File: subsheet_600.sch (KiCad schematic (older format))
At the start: 9 parts, among them U600 SIMM_30_PHY, U601 SIMM_30_PHY, U602 SIMM_30_PHY, U603 SIMM_30_PHY

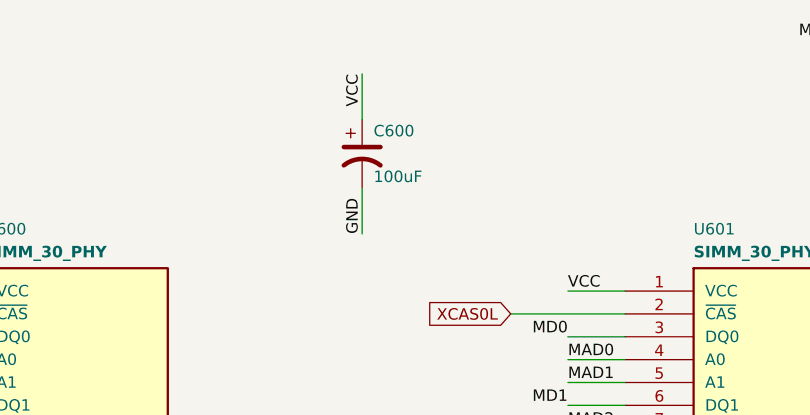
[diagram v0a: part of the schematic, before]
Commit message: Resolves #12 : Use the reference 'CP?' for polarized capacitors
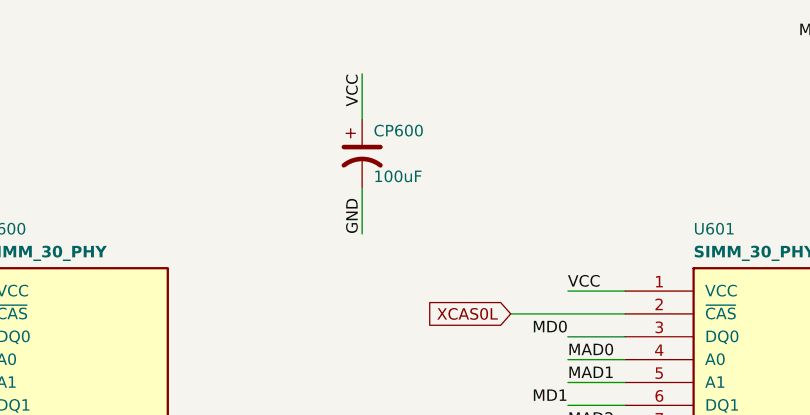
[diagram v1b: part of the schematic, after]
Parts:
- renumbered C600 to CP600
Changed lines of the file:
@@
 AR Path="/60CC3B10/60D4F85E" Ref="C?"  Part="1"
 AR Path="/60CD36E9/60D4F85E" Ref="C?"  Part="1"
-AR Path="/60CE6C60/60D4F85E" Ref="C600"  Part="1"
-F 0 "C600" H 4300 1600 50  0000 L CNN
+AR Path="/60CE6C60/60D4F85E" Ref="CP600"  Part="1"
+F 0 "CP600" H 4300 1600 50  0000 L CNN
 F 1 "100uF" H 4300 1400 50  0000 L CNN
 F 2 "commons_passives_THT:Passive_THT_capacitor_polarized_W6.35mm_L20.32mm" H 4250 1500 50  0001 C CNN

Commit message: Resolves #8 : Assign 1206 hand-solder footprints to non polarized capacitors
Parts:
- C633, C634, C635, C636: footprint commons_passives_THT:Passive_THT_capacitor_mlcc_W2.54mm_L10.16mm -> Capacitor_SMD:C_1206_3216Metric_Pad1.33x1.80mm_HandSolder
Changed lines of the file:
@@
 F 0 "C633" H 1275 3600 50  0000 L CNN
 F 1 "0.22uF" H 1275 3400 50  0000 L CNN
-F 2 "commons_passives_THT:Passive_THT_capacitor_mlcc_W2.54mm_L10.16mm" H 1288 3350 50  0001 C CNN
+F 2 "Capacitor_SMD:C_1206_3216Metric_Pad1.33x1.80mm_HandSolder" H 1288 3350 50  0001 C CNN
 F 3 "~" H 1250 3500 50  0001 C CNN
 	1    1250 3500
@@
 F 0 "C635" H 7025 3600 50  0000 L CNN
 F 1 "0.22uF" H 7025 3400 50  0000 L CNN
-F 2 "commons_passives_THT:Passive_THT_capacitor_mlcc_W2.54mm_L10.16mm" H 7038 3350 50  0001 C CNN
+F 2 "Capacitor_SMD:C_1206_3216Metric_Pad1.33x1.80mm_HandSolder" H 7038 3350 50  0001 C CNN
 F 3 "~" H 7000 3500 50  0001 C CNN
 	1    7000 3500
@@
 F 0 "C634" H 1275 7600 50  0000 L CNN
 F 1 "0.22uF" H 1275 7400 50  0000 L CNN
-F 2 "commons_passives_THT:Passive_THT_capacitor_mlcc_W2.54mm_L10.16mm" H 1288 7350 50  0001 C CNN
+F 2 "Capacitor_SMD:C_1206_3216Metric_Pad1.33x1.80mm_HandSolder" H 1288 7350 50  0001 C CNN
 F 3 "~" H 1250 7500 50  0001 C CNN
 	1    1250 7500
@@
 F 0 "C636" H 7025 7600 50  0000 L CNN
 F 1 "0.22uF" H 7025 7400 50  0000 L CNN
-F 2 "commons_passives_THT:Passive_THT_capacitor_mlcc_W2.54mm_L10.16mm" H 7038 7350 50  0001 C CNN
+F 2 "Capacitor_SMD:C_1206_3216Metric_Pad1.33x1.80mm_HandSolder" H 7038 7350 50  0001 C CNN
 F 3 "~" H 7000 7500 50  0001 C CNN
 	1    7000 7500

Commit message: Resolves #9 : Assign radial THT footprints to polarized capacitors
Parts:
- CP600: footprint commons_passives_THT:Passive_THT_capacitor_polarized_W6.35mm_L20.32mm -> Capacitor_THT:C_Radial_D8.0mm_H11.5mm_P3.50mm
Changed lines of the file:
@@
 F 0 "CP600" H 4300 1600 50  0000 L CNN
 F 1 "100uF" H 4300 1400 50  0000 L CNN
-F 2 "commons_passives_THT:Passive_THT_capacitor_polarized_W6.35mm_L20.32mm" H 4250 1500 50  0001 C CNN
+F 2 "Capacitor_THT:C_Radial_D8.0mm_H11.5mm_P3.50mm" H 4250 1500 50  0001 C CNN
 F 3 "~" H 4250 1500 50  0001 C CNN
 	1    4250 1500
